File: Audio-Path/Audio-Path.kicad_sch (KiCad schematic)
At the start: 52 parts, among them IC252 BA15218, IC253 BA15218, J501B L, J501C R_SW

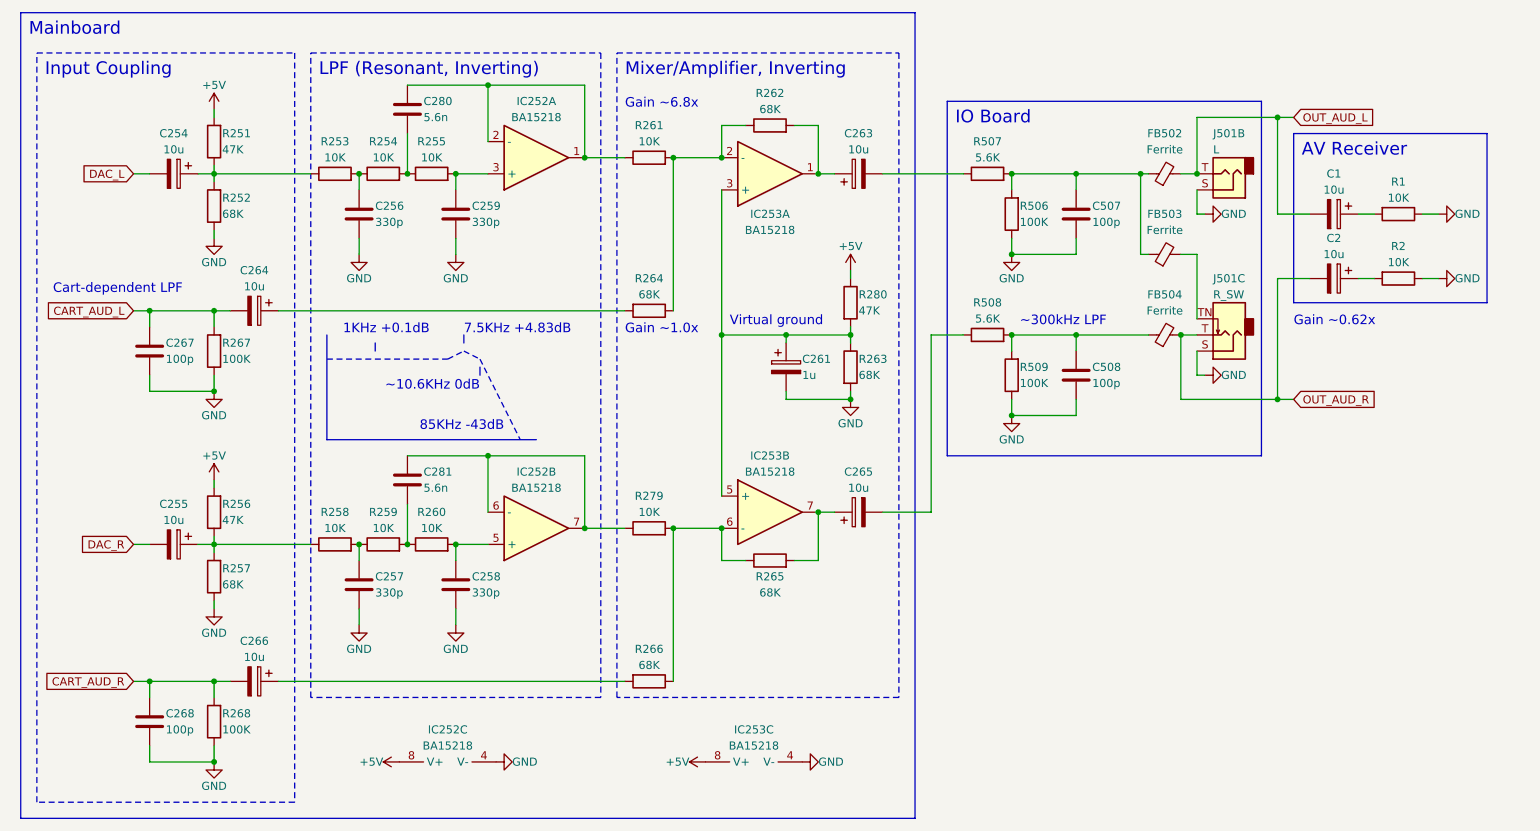
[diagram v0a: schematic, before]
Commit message: Update all to Kicad 9.0 and cleanup
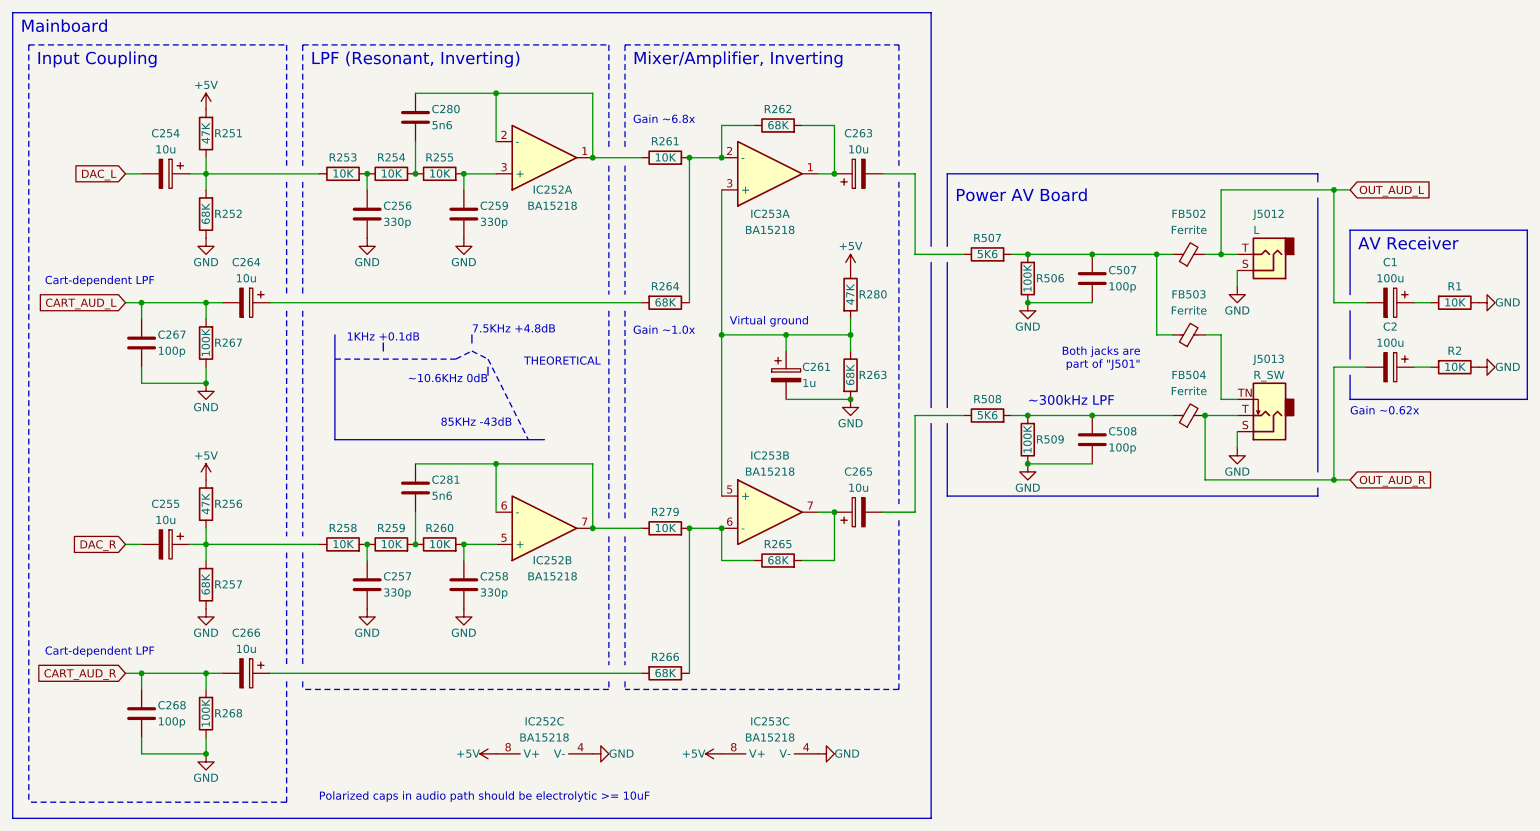
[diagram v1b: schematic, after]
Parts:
- C1, C2: value 10u -> 100u
- C280, C281: value 5.6n -> 5n6
- R507, R508: value 5.6K -> 5K6
- renumbered J501B to J5012, J501C to J5013
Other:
- note added: "7.5KHz +4.8dB"
- note added: "Both jacks are part of "J501""
- note added: "Polarized caps in audio path should be electrolytic >= 10uF"
- note added: "Power AV Board"
- note added: "THEORETICAL"
- note removed: "7.5KHz +4.83dB"
- note removed: "IO Board"
- moved on the sheet: C1, C2, C254, C255, C256, C257, C258, C259, C261, C264, C266, C267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
